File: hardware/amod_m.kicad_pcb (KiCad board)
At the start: 4 copper layers, 100 x 100 mm, 207 parts, among them J1001 SMA, J101 USB-C, J102 rails, J1101 SMA, J1102 cell, J201 SMA, J202 5-16V, J301 SMA, J302 SMA, J303 motor, J304 Pmod, J401 SMA, J402 SMA, J403 stepper, J501 SMA, J502 SMA, J503 servo, J601 SMA, J602 SMA, J603 SMA, J604 coil, J605 D Z, J701 SMA, J702 SMA, J703 load, J801 SMA, J802 SMA, J803 SMA, J804 out, J901 SMA, Q1001 AO3401A, Q301 AO3401A, Q401 AO3401A, Q501 AO3401A, Q601 AO3401A, Q602 NCE6020AK, Q801 AO3401A, Q802 AO3400A, Q803 AO3400A, Q901 AO3401A, SW1001 ON, SW301 ON, SW401 ON, SW501 ON, SW601 ON, SW801 ON, SW901 ON, U1001 QRE1113, U1002 OPA810, U101 LM2664, U102 3.3V, U1101 INA828, U301 DRV8251A, U302 OPA2171, U303 3.3V, U401 DRV8251A, U402 DRV8251A, U501 TLV3501, U502 INA181, U601 TLV3501, U602 INA181, U701 TCA0372, U702 INA181, U703 OPA810, U801 TLV3501, U802 TPS28225, U803 INA181, U901 DRV5055, U902 OPA810

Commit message: AMOD-M: the back panels, the Pmod lines, the handbook, the dead-on-arrival list; AMOD-C and AMOD-M in the README's table
Each tile's back says what to know while cabling it (the encoder's PH order, the
stepper's XH, the servo header, the solenoid's jumper, the linear amplifier's
watt); tile_docs gains AMOD-M's eleven entries and the motor chips' pages.
m7's clipping plot found no room beside the QR code and was dropped.

Co-Authored-By: Claude Opus 5.5 <noreply@anthropic.com>
Claude-Session: https://claude.ai/code/session_01RKeoKvFFzjk3cEBLCXXHnB
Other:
- board text added: "+-85 mT"
- board text added: "+3.3 V 300 mA"
- board text added: "+5 V 1.5 A"
- board text added: "-5 V 40 mA"
- board text added: "1 A per coil"
- board text added: "1 W in the chip:"
- board text added: "1 red E+ 2 black E-"
- board text added: "2 A limit"
- board text added: "2-3: 24 V TVS"
- board text added: "3 white S-"
- board text added: "4 green S+"
- board text added: "5-16 V, centre +"
- board text added: "8 ohm at 5-6 V"
- board text added: "9.75 mV/mT"
- board text added: "A: IN1 IO2, IN2 IO3"
- board text added: "B: IN1 IO4, IN2 IO8"
- board text added: "CMD 1-2 ms / 20 ms"
- board text added: "CMD high: coil on"
- board text added: "I 0.98 V/A"
- board text added: "I 1 V/A"
- board text added: "I 1 V/A both ways"
- board text added: "I 1 V/A, VO /16"
- board text added: "IN +-1 V"
- board text added: "IN1 IO7, IN2 IO1"
- board text added: "OUT 0.1-0.9 V"
- board text added: "PH: M1 G A B 3V3 M2"
- board text added: "PWM 100-500 kHz"
- board text added: "USB-C 5 V only"
- board text added: "V = motor / 13"
- board text added: "VD = drain / 52"
- board text added: "VMOT = in - 0.4 V"
- board text added: "VO = duty x VMOT"
- board text added: "XH: A+ A- B+ B-"
- board text added: "gain 201"
- board text added: "header: S + -"
- board text added: "jumper 1-2: diode"
- board text added: "load = 4 x IN"
- board text added: "load up to 1 A"
- board text added: "m1 Power"
- board text added: "m10 Optical"
- board text added: "m11 Load cell"
- board text added: "m2 Motor supply"
- board text added: "m3 DC motor"
- board text added: "m4 Stepper"
- board text added: "m5 Servo"
- board text added: "m6 Solenoid"
- board text added: "m7 Linear amp"
- board text added: "m8 Buck stage"
- board text added: "m9 Hall"
- board text added: "none: avalanche"
- board text added: "not switched"
- board text added: "or USB 5 V alone"
- board text added: "sensor top left"
- board text added: "target 1 mm up"

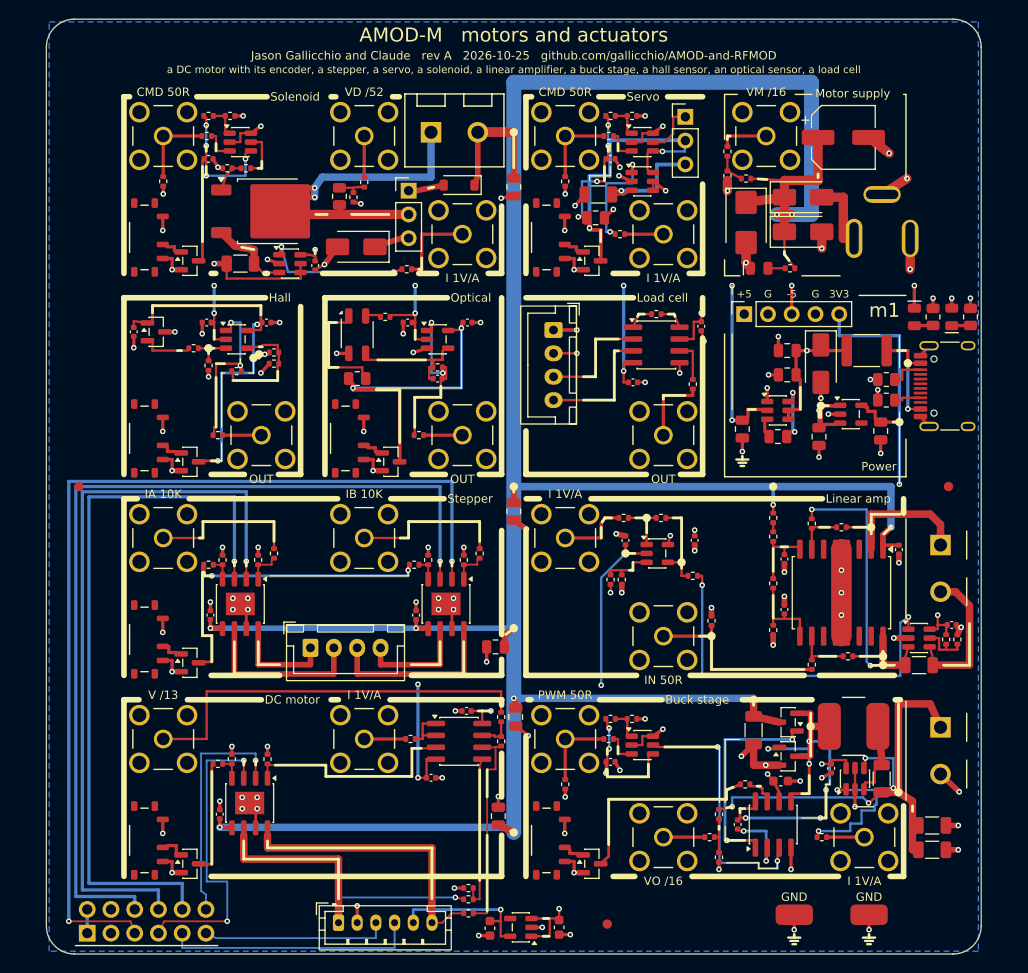
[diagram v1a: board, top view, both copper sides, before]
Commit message: Pre-order checks from CLAUDE_PCB.md's new lessons (Prompt 21): the KF301 terminals turned for their wire openings (CPL +180, body 3.7 / 4.0, a wire-face check), four oversold parts swapped (27R, 6.8k, 220n, OPA847IDBVT at its own +180), fourteen vias moved out of SMD pads (check_layout.py gates it and RF detours), 200-250 mW terminations, assembly drawings from Fab and silk fitted to Letter (fit_pdf.py from CostasLink), the stock gate on JLCPCB's free count, electrolytics in the rotation check, the RF gates surveyed (rf_extract.py, rf_survey.py) and written into the DOA lists; all nine boards rebuilt: ERC 0, DRC 0, every check
Co-Authored-By: Claude Opus 5.5 <noreply@anthropic.com>
Claude-Session: https://claude.ai/code/session_01RKeoKvFFzjk3cEBLCXXHnB
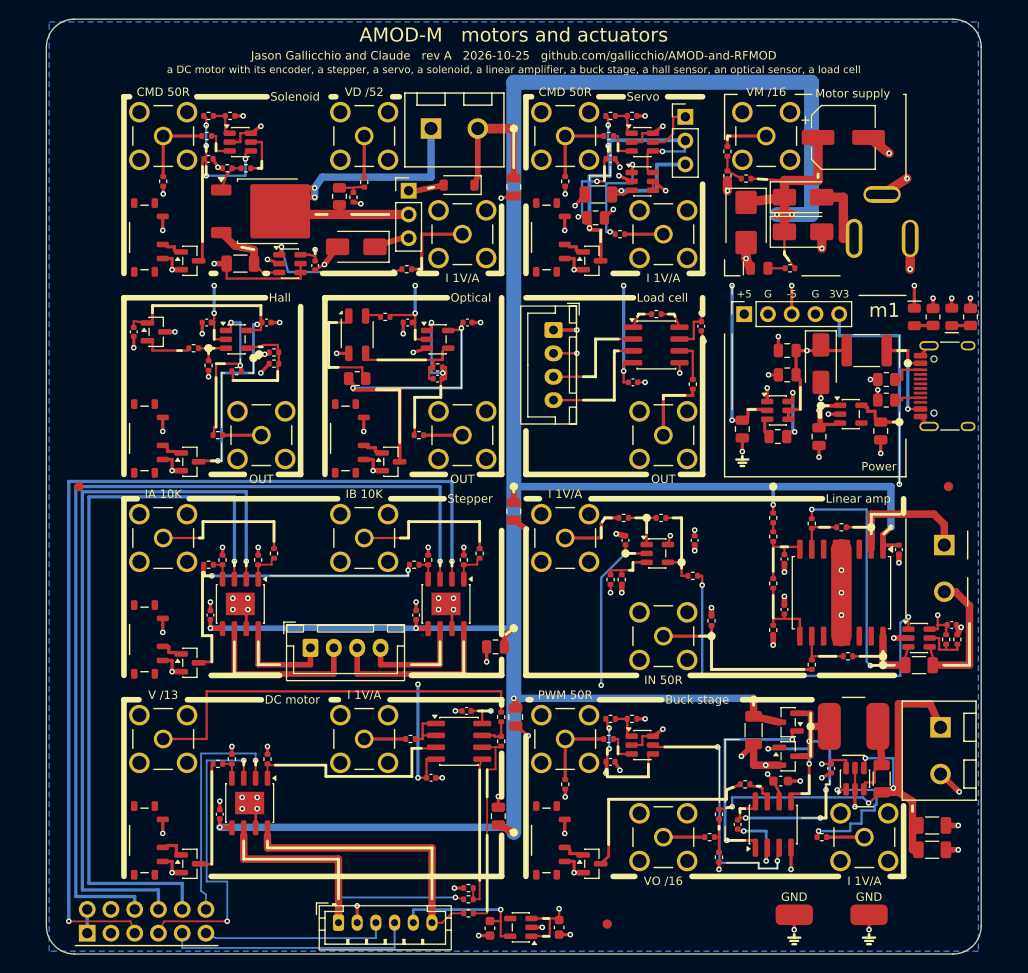
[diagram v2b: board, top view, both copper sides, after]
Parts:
- moved J604 0.40 mm to (43.6, 11.7)
- moved J703 0.40 mm to (96.0, 58.8)
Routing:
- net /VMOT: track 363.9 -> 364.7 mm
